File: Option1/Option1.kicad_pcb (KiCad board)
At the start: 2 copper layers, 86 x 62 mm, 114 parts, among them J1501 GH-13AB, J1801 Conn_01x08_Socket, J401 Conn_01x05_Pin, J402 Conn_01x04_Pin, J403 Conn_01x05_Pin, J503 KF2EDGKRG-3.5-2*7P, Q1001 JY2302, Q1101 JY2302, Q1401 BC817-40, Q1402 BC817-40, Q601 JY2302, Q901 JY2302, SW401 4*4*1.7, U1401 CH340X, U1601 W25Q512JVEIQ, U1701 TJA1051T-3, U201 U7812-500, U202 K7805-500R2_C909663, U203 SY8089AAAC, U204 SY8089AAAC, U301 TJA1051T-3, U302 MCP2515-I/ST, U801 ESP32-WROOM-32E-N4, U802 MCP23017_SO, X301 XL1EL89CSI-111YLC-8M

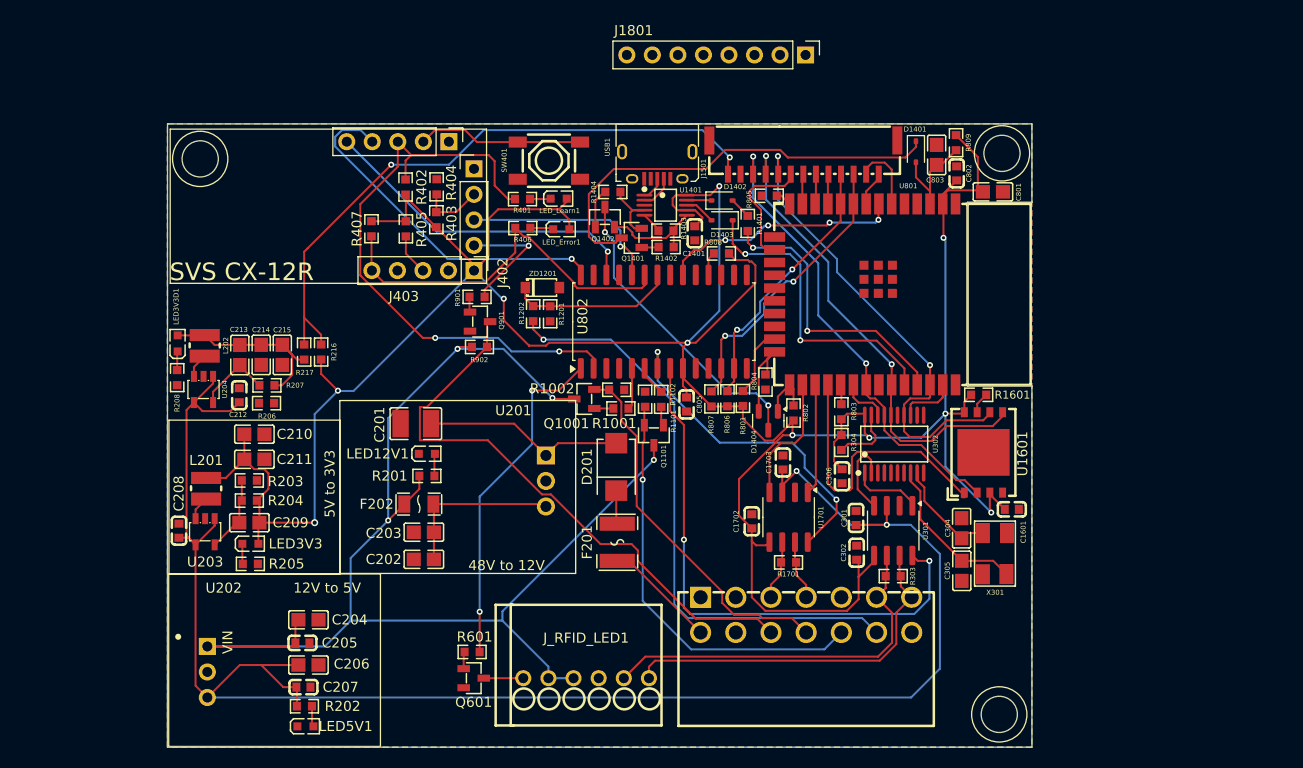
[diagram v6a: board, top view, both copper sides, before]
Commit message: EasyEDA Lib in Projekt verschoben; Footprints, Silkscreen für designrule angepasst; Bauteilbeschriftungen entfernt, müssen neu angeordnet werden, JLC Rules eingebunden, Designrules erfolgreich bis auf Beschriftungen, Fehler in Radio Controll Beschaltung behoben; RFID Pinheader hinzugefügt
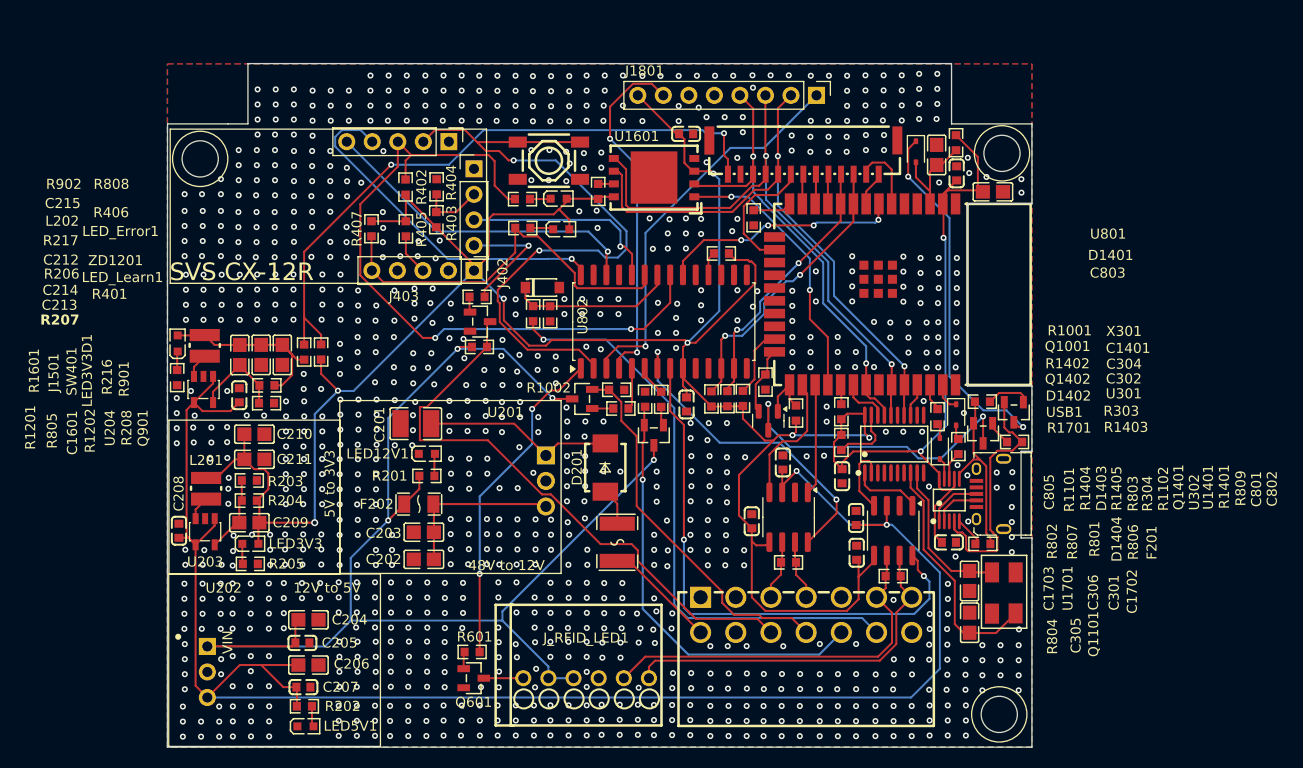
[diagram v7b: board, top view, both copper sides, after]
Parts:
- added R1405: 500Ω, easyeda2kicad:R0603, F.Cu at (178.6, 82.1)
- D201: footprint easyeda2kicad:SMB_L4.6-W3.6-LS5.3-RD -> easyeda2kicad:SMB_L4.6-W3.6-LS5.3-R-RD
- moved C1601 49.4 mm to (151.5, 51.0)
- moved R1404 47.1 mm to (184.2, 81.6)
- moved USB1 46.5 mm to (181.8, 86.8), turned to 90 degrees
- moved R1403 44.3 mm to (181.1, 91.8)
- moved Q1402 43.3 mm to (181.1, 80.8), turned to 90 degrees
- moved R1601 42.9 mm to (142.8, 56.7), turned to -90 degrees
- moved U1601 42.7 mm to (148.3, 55.3), turned to 180 degrees
- moved Q1401 41.8 mm to (184.1, 78.7), turned to 90 degrees
- moved U1401 40.7 mm to (177.7, 87.4), turned to 0 degrees
- moved C1401 39.8 mm to (177.7, 91.6), turned to 0 degrees
- moved R1402 35.0 mm to (181.0, 77.6), turned to 0 degrees
- moved D1402 32.8 mm to (176.8, 82.3), turned to 90 degrees
- moved D1403 30.3 mm to (178.4, 78.9), turned to -90 degrees
- moved R1401 26.9 mm to (176.6, 79.1), turned to 90 degrees
- moved C304 5.31 mm to (179.7, 95.4), turned to 90 degrees
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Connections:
- D1403 pad 1: RXD0 -> IO23
- J1501 pad 9: IO22 -> IO3
- J1801 pad 2: IO22 -> IO3
- R1401 pad 2: TXD0 -> IO22
- U1401 pad 8: Net-(D1403-A) -> Net-(U1401-TXD)
- U1601 pad 6: IO22 -> IO3
- U302 pad 13: IO23 -> IO1
- U302 pad 14: IO22 -> IO3
- U801 pad 34: RXD0 -> IO3
- U801 pad 35: TXD0 -> IO1
- U802 pad 2: LED_Modus -> Lernmodus
- U802 pad 21: unconnected-(U802-GPA0-Pad21) -> LED_Modus
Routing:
- net IO3: track 0.00 -> 61.3 mm, vias 0 -> 2
- net Lernmodus: track 16.6 -> 67.5 mm, vias 0 -> 2
- net IO22: track 47.3 -> 2.83 mm, vias 2 -> 0
- net /MCT  Wlan/SPI_CS_RFID: track 0.00 -> 39.4 mm, vias 0 -> 1
- net /MCT  Wlan/SPI_RST_RFID: track 0.00 -> 35.3 mm, vias 0 -> 2
- net RXD0: track 30.6 -> 0.00 mm, vias 2 -> 0
- net TXD0: track 28.5 -> 0.00 mm, vias 2 -> 0
- net Net-(U1401-~{RTS}): track 7.48 -> 25.1 mm
- net IO21: track 46.8 -> 60.2 mm
- net LED_Modus: track 60.6 -> 70.6 mm
- net Net-(U302-OSC2): track 15.8 -> 24.1 mm
- net Net-(D1401-K): track 43.6 -> 35.9 mm, vias 0 -> 2
- net Net-(U1401-TNOW/~{DTR}): track 10.5 -> 18.2 mm
- net Net-(U302-OSC1): track 10.7 -> 15.3 mm
- net IO1: track 0.00 -> 3.29 mm
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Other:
- board size 86 x 62 mm -> 86 x 68 mm
- board text added: "12V"
- board text added: "3V3"
- board text added: "48V_Fused"
- board text added: "48V_IN"
- board text added: "5V"
- board text added: "CAN1_H"
- board text added: "CAN1_L"
- board text added: "CAN2_H"
- board text added: "CAN2_L"
- board text added: "F2_Select"
- board text added: "Fehler_LED"
- board text added: "GND"
- board text added: "LED-IN_VCU"
- board text added: "Lernmodus"
- board text added: "Modus_LED"
- board text added: "Notaus_VCU"
- board text added: "RFID_12V"
- board text added: "RFID_CAN2_H"
- board text added: "RFID_CAN2_L"
- board text added: "RFID_GND"
- board text added: "RX_CH1"
- board text added: "RX_CH2"
- board text added: "RX_CH3"
- board text added: "RX_CH4"
- board text added: "RemoteDrive VCU"
- board text added: "SMS Revo SL - Option1 - V1.0"
- board text added: "SOC_VCU"
- board text added: "SPI_CLK"
- board text added: "SPI_CS"
- board text added: "SPI_MISO"
- board text added: "SPI_MOSI"
- board text added: "SPI_RST"
- board text added: "Status-LED +"
- board text added: "Status-LED -"
- board text added: "TX_Analog"
- board text added: "USB"
- board text added: "X"

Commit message: Leiterbahndicke hinzugefügt, Via-Dicke angepasst, Bauteil referenzen hinzugefügt
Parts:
- J401, J403: footprint Connector_PinHeader_2.54mm:PinHeader_1x05_P2.54mm_Vertical -> easyeda2kicad:PinHeader_1x05_P2.54mm_Vertical
- J402: footprint Connector_PinHeader_2.54mm:PinHeader_1x04_P2.54mm_Vertical -> easyeda2kicad:PinHeader_1x04_P2.54mm_Vertical
- renumbered LED3V3D1 to 3V3D, C801 to 801, USB1 to USB
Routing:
- net 3.3V: track 309.7 -> 310.7 mm
- net /Powersupply/3.3V_D1: track 19.2 -> 19.8 mm
- net GND: vias 1022 -> 1017
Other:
- board size 86 x 68 mm -> 86 x 69.5 mm
- board text added: "I: SW GE GN RO VI BL OR"
- board text added: "II: SW GE GN RO VI BL OR"
